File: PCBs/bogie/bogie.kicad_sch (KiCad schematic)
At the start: 2 parts

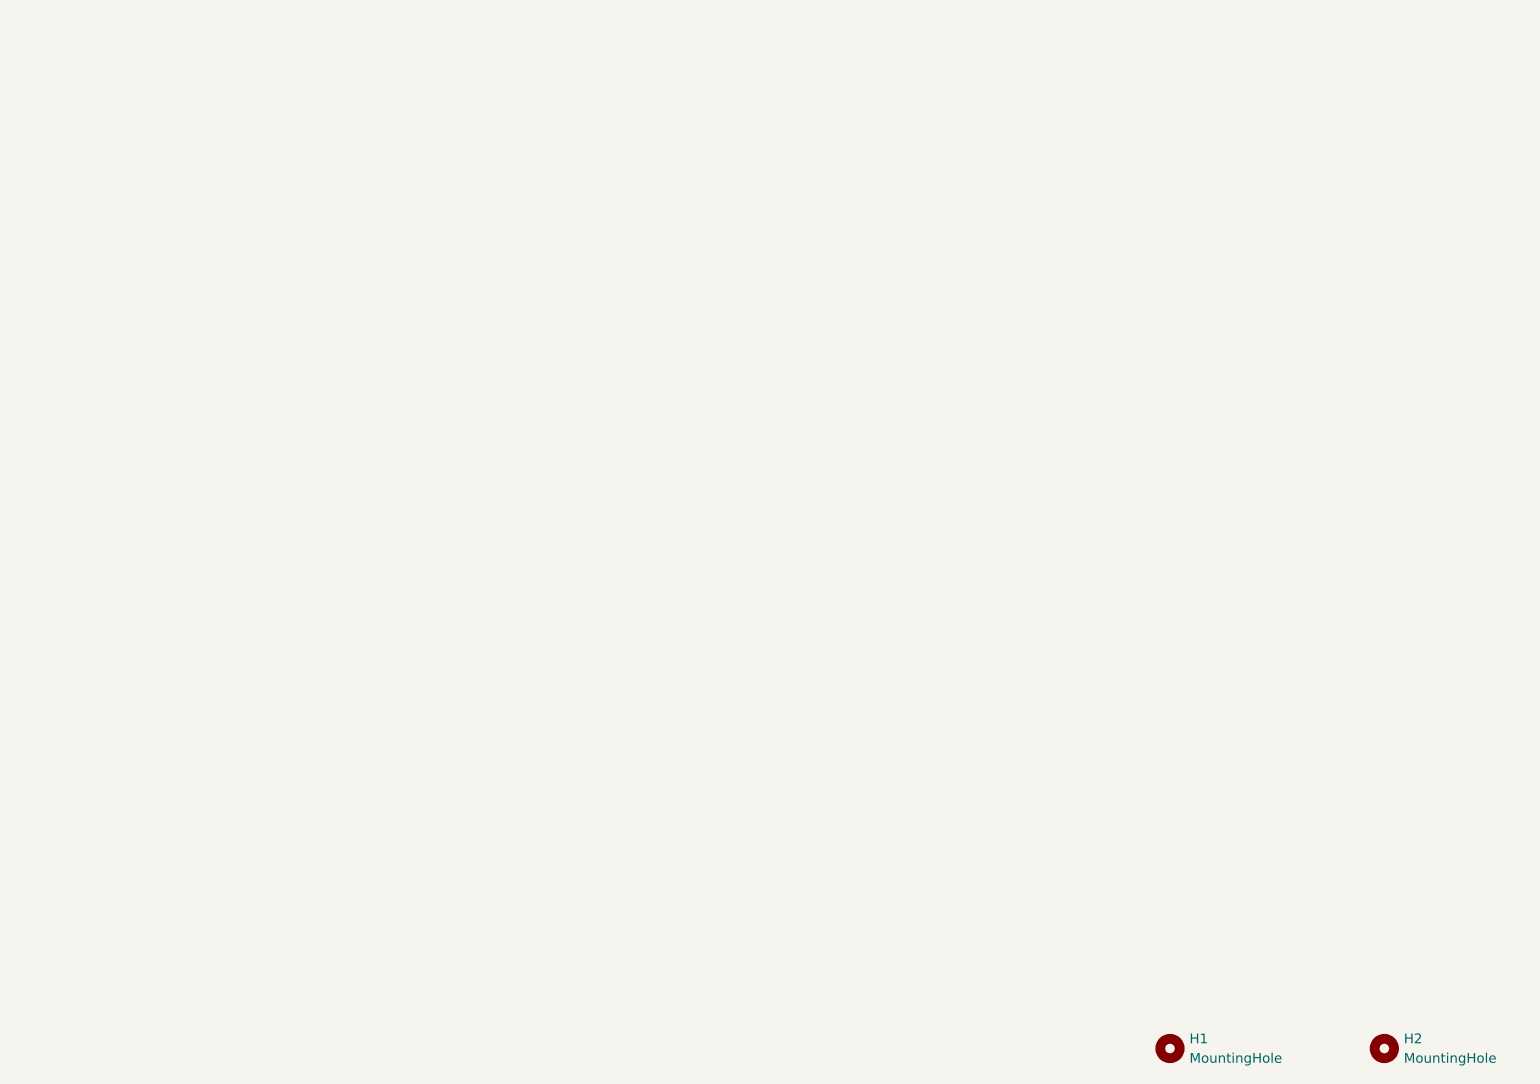
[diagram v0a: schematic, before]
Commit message: Torso, bogie and rail complete. Next up: revise hand and IMU board in conjunction
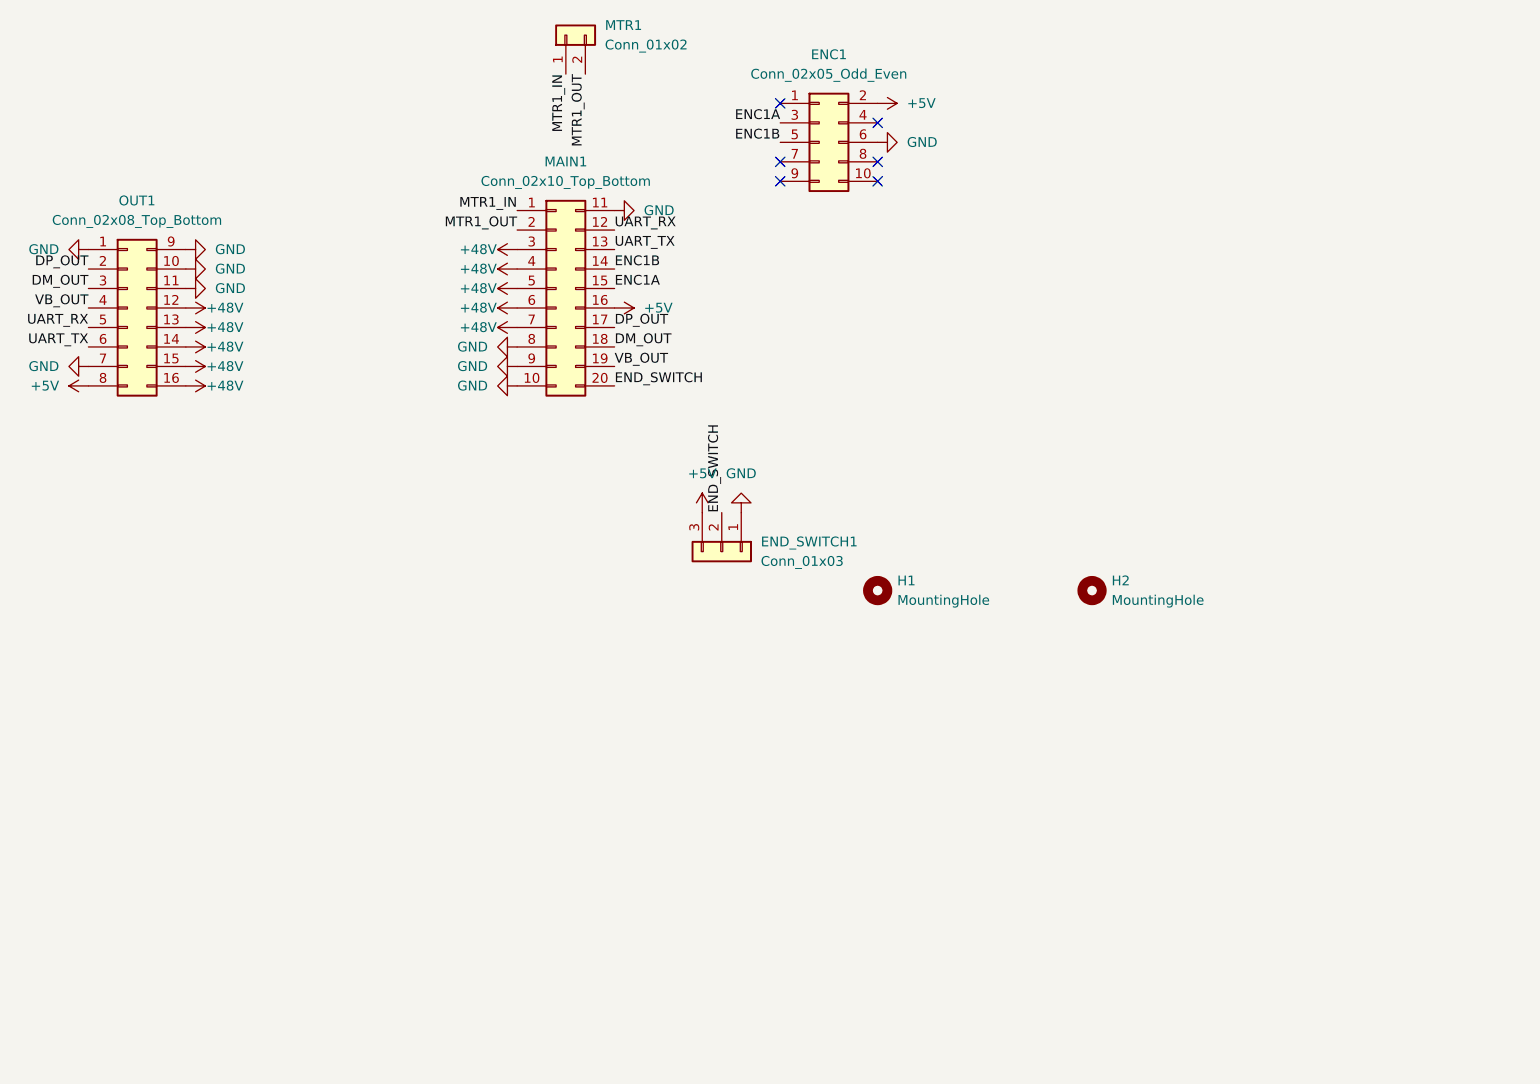
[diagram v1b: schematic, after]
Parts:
- added ENC1: Conn_02x05_Odd_Even, Connector_PinHeader_2.54mm:PinHeader_2x05_P2.54mm_Vertical, symbol Connector_Generic:Conn_02x05_Odd_Even
- added END_SWITCH1: Conn_01x03, Connector_PinHeader_2.54mm:PinHeader_1x03_P2.54mm_Vertical, symbol Connector_Generic:Conn_01x03
- added MAIN1: Conn_02x10_Top_Bottom, 1761681-7:1761681-7_TYC, symbol Connector_Generic:Conn_02x10_Top_Bottom
- added MTR1: Conn_01x02, 70543-0001:70543-0001_MOL, symbol Connector_Generic:Conn_01x02
- added OUT1: Conn_02x08_Top_Bottom, 2-1761603-6:2-1761603-6_TYC, symbol Connector_Generic:Conn_02x08_Top_Bottom
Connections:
- new net +48V: MAIN1.3 (Pin_3), MAIN1.4 (Pin_4), MAIN1.5 (Pin_5), MAIN1.6 (Pin_6), MAIN1.7 (Pin_7), OUT1.12 (Pin_12), OUT1.13 (Pin_13), OUT1.14 (Pin_14), OUT1.15 (Pin_15), OUT1.16 (Pin_16)
- new net +5V: ENC1.2 (Pin_2), END_SWITCH1.3 (Pin_3), MAIN1.16 (Pin_16), OUT1.8 (Pin_8)
- new net DM_OUT: MAIN1.18 (Pin_18), OUT1.3 (Pin_3)
- new net DP_OUT: MAIN1.17 (Pin_17), OUT1.2 (Pin_2)
- new net ENC1A: ENC1.3 (Pin_3), MAIN1.15 (Pin_15)
- new net ENC1B: ENC1.5 (Pin_5), MAIN1.14 (Pin_14)
- new net END_SWITCH: END_SWITCH1.2 (Pin_2), MAIN1.20 (Pin_20)
- new net GND: ENC1.6 (Pin_6), END_SWITCH1.1 (Pin_1), MAIN1.10 (Pin_10), MAIN1.11 (Pin_11), MAIN1.8 (Pin_8), MAIN1.9 (Pin_9), OUT1.1 (Pin_1), OUT1.10 (Pin_10), OUT1.11 (Pin_11), OUT1.7 (Pin_7), OUT1.9 (Pin_9)
- new net MTR1_IN: MAIN1.1 (Pin_1), MTR1.1 (Pin_1)
- new net MTR1_OUT: MAIN1.2 (Pin_2), MTR1.2 (Pin_2)
- new net UART_RX: MAIN1.12 (Pin_12), OUT1.5 (Pin_5)
- new net UART_TX: MAIN1.13 (Pin_13), OUT1.6 (Pin_6)
- new net VB_OUT: MAIN1.19 (Pin_19), OUT1.4 (Pin_4)
- no-connect marks 0 -> 6
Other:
- moved on the sheet: H1, H2

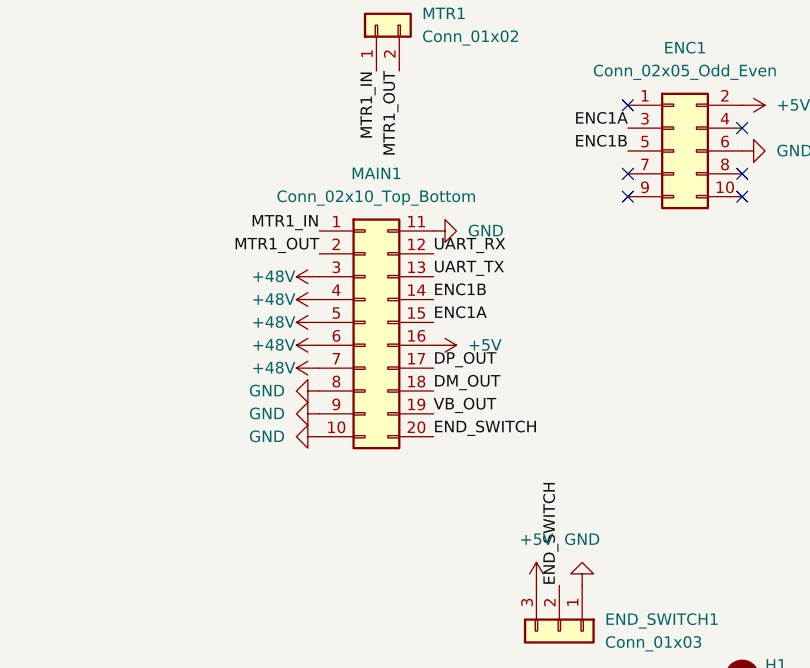
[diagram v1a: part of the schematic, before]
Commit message: Working UART input for basic control. All motors work. Next up: switch interrupts
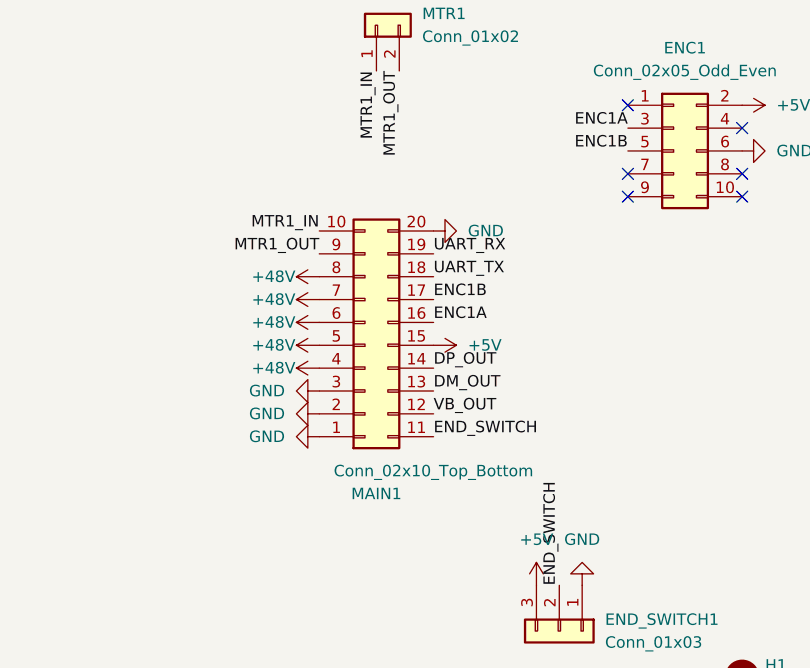
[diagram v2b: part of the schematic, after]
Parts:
- H1, H2: footprint MountingHole:MountingHole_3.5mm -> MountingHole:MountingHole_3.7mm
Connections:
- net +48V: now also MAIN1.8 (Pin_8); no longer MAIN1.3 (Pin_3)
- net +5V: now also MAIN1.15 (Pin_15); no longer MAIN1.16 (Pin_16)
- net DM_OUT: now also MAIN1.13 (Pin_13); no longer MAIN1.18 (Pin_18)
- net DP_OUT: now also MAIN1.14 (Pin_14); no longer MAIN1.17 (Pin_17)
- net ENC1A: now also MAIN1.16 (Pin_16); no longer MAIN1.15 (Pin_15)
- net ENC1B: now also MAIN1.17 (Pin_17); no longer MAIN1.14 (Pin_14)
- net END_SWITCH: now also MAIN1.11 (Pin_11); no longer MAIN1.20 (Pin_20)
- net GND: now also MAIN1.1 (Pin_1), MAIN1.2 (Pin_2), MAIN1.20 (Pin_20), MAIN1.3 (Pin_3); no longer MAIN1.10 (Pin_10), MAIN1.11 (Pin_11), MAIN1.8 (Pin_8), MAIN1.9 (Pin_9)
- net MTR1_IN: now also MAIN1.10 (Pin_10); no longer MAIN1.1 (Pin_1)
- net MTR1_OUT: now also MAIN1.9 (Pin_9); no longer MAIN1.2 (Pin_2)
- net UART_RX: now also MAIN1.19 (Pin_19); no longer MAIN1.12 (Pin_12)
- net UART_TX: now also MAIN1.18 (Pin_18); no longer MAIN1.13 (Pin_13)
- net VB_OUT: now also MAIN1.12 (Pin_12); no longer MAIN1.19 (Pin_19)
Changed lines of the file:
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@@
       (effects (font (size 1.27 1.27)) (justify left))
     )
-    (property "Footprint" "MountingHole:MountingHole_3.5mm" (at 146.05 97.79 0)
+    (property "Footprint" "MountingHole:MountingHole_3.7mm" (at 146.05 97.79 0)
       (effects (font (size 1.27 1.27)) hide)
     )
@@
     )
   )
-  (symbol (lib_id "Connector_Generic:Conn_02x10_Top_Bottom") (at 104.14 58.42 0) (unit 1)
-    (in_bom yes) (on_board yes) (dnp no) (fields_autoplaced)
-    (property "Reference" "MAIN1" (at 105.41 41.91 0)
-      (effects (font (size 1.27 1.27)))
-    )
-    (property "Value" "Conn_02x10_Top_Bottom" (at 105.41 44.45 0)
-      (effects (font (size 1.27 1.27)))
-    )
-    (property "Footprint" "1761681-7:1761681-7_TYC" (at 104.14 58.42 0)
-      (effects (font (size 1.27 1.27)) hide)
-    )
-    (property "Datasheet" "~" (at 104.14 58.42 0)
+  (symbol (lib_id "Connector_Generic:Conn_02x10_Top_Bottom") (at 104.14 60.96 0) (mirror x) (unit 1)
+    (in_bom yes) (on_board yes) (dnp no)
+    (property "Reference" "MAIN1" (at 105.41 77.47 0)
+      (effects (font (size 1.27 1.27)))
+    )
+    (property "Value" "Conn_02x10_Top_Bottom" (at 111.76 74.93 0)
+      (effects (font (size 1.27 1.27)))
+    )
+    (property "Footprint" "1761681-7:1761681-7_TYC" (at 104.14 60.96 0)
+      (effects (font (size 1.27 1.27)) hide)
+    )
+    (property "Datasheet" "~" (at 104.14 60.96 0)
       (effects (font (size 1.27 1.27)) hide)
     )
@@
       (effects (font (size 1.27 1.27)) (justify left))
     )
-    (property "Footprint" "MountingHole:MountingHole_3.5mm" (at 173.99 97.79 0)
-      (effects (font (size 1.27 1.27)) hide)
-    )
+    (property "Footprint" "MountingHole:MountingHole_3.7mm" (at 173.99 97.79 0)
+      (effects (font (size 1.27 1.27)) hide)
+    )

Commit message: merged changes from timertests, mostly documentation and such. Did not add tim6 config
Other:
- title: (none) -> Bogie PCB
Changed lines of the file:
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@@
 (kicad_sch (version 20230121) (generator eeschema)
   (paper "A5")
+  (title_block
+    (title "Bogie PCB")
+    (rev "Mk1.2")
+  )
   (no_connect (at 146.05 41.91))
   (no_connect (at 133.35 44.45))
